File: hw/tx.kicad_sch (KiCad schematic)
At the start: 60 parts, among them Q301 MMBF170, Q302 MMBF170, Q303 MMBF170, Q304 MMBF170, Q305 MMBF170, Q306 MMBF170, Q307 MMBF170, Q308 MMBF170, Q309 MMBF170, Q310 MMBF170, Q311 MMBF170, Q312 MMBF170, T301 BN-43-202_DualPri_CTSec, U301 ICE40UP5K-SG48ITR, U302 CD74ACT541SM96, Y301 40MHz

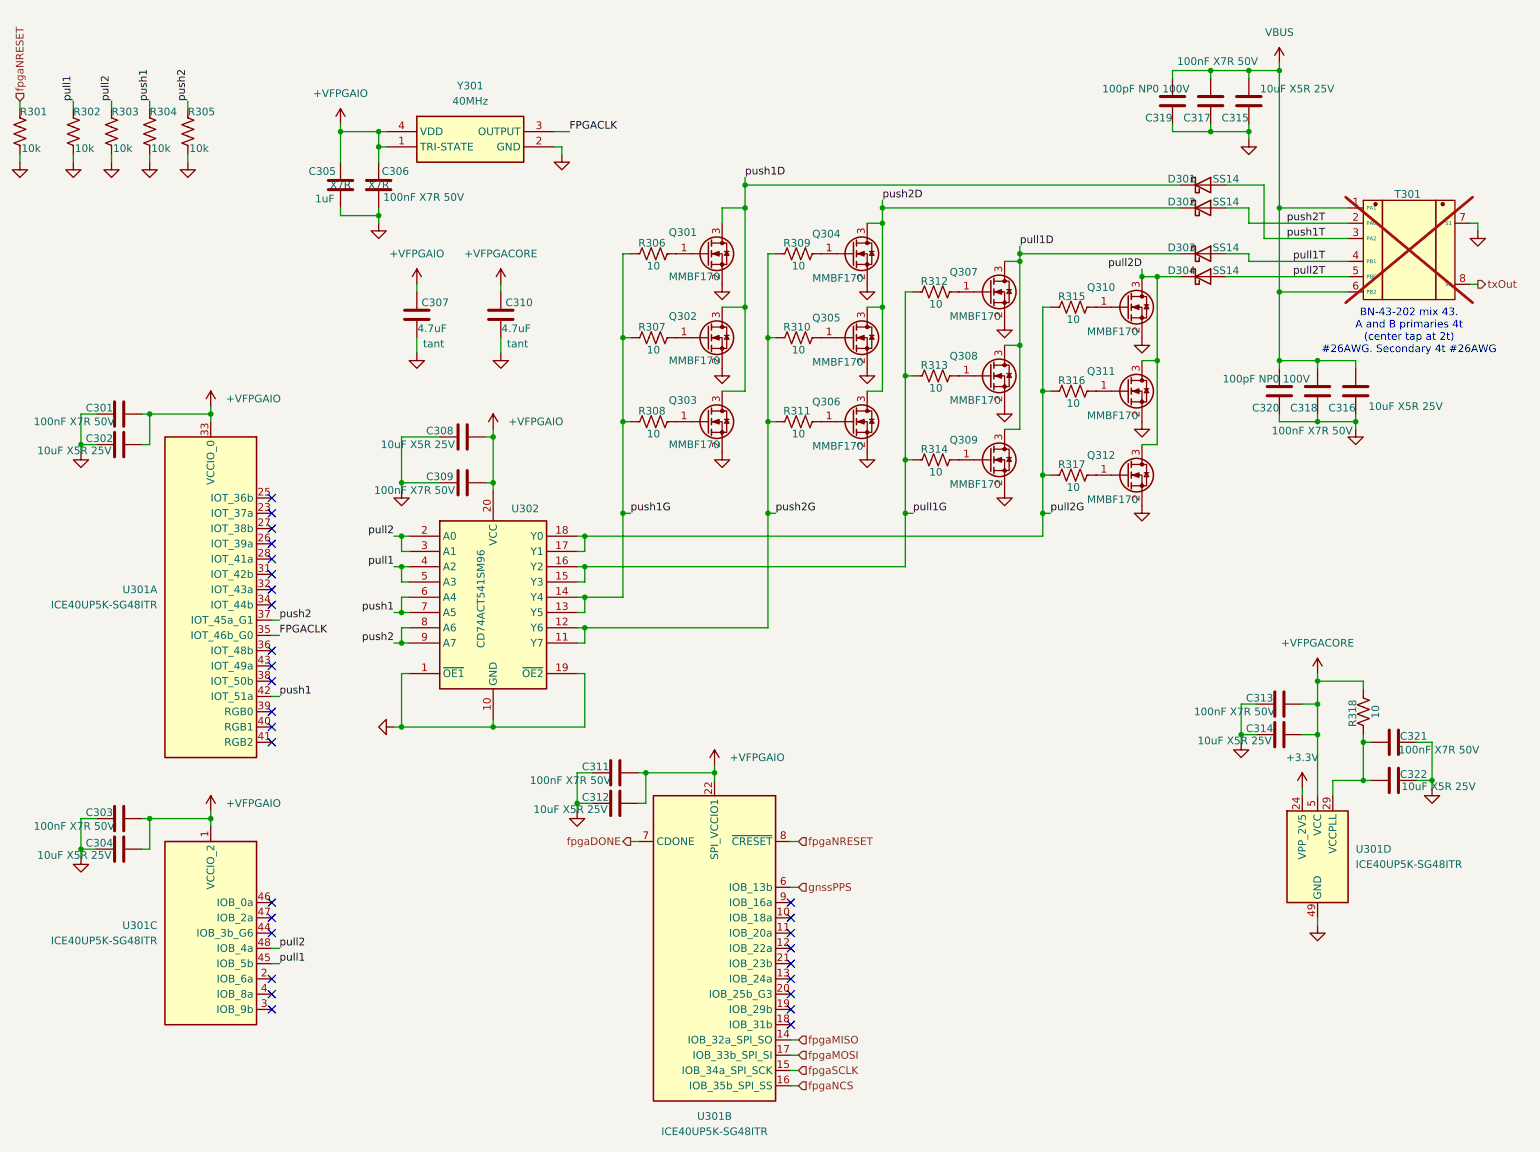
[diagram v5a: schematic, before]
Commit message: Still working on FPGA config loading. Problem is now CMOS lockup caused by FPGACORE vs FPGAIO rails. I moved FPGAIO enable to IO42 on ESP32 and pgFPGACORE to IO41.
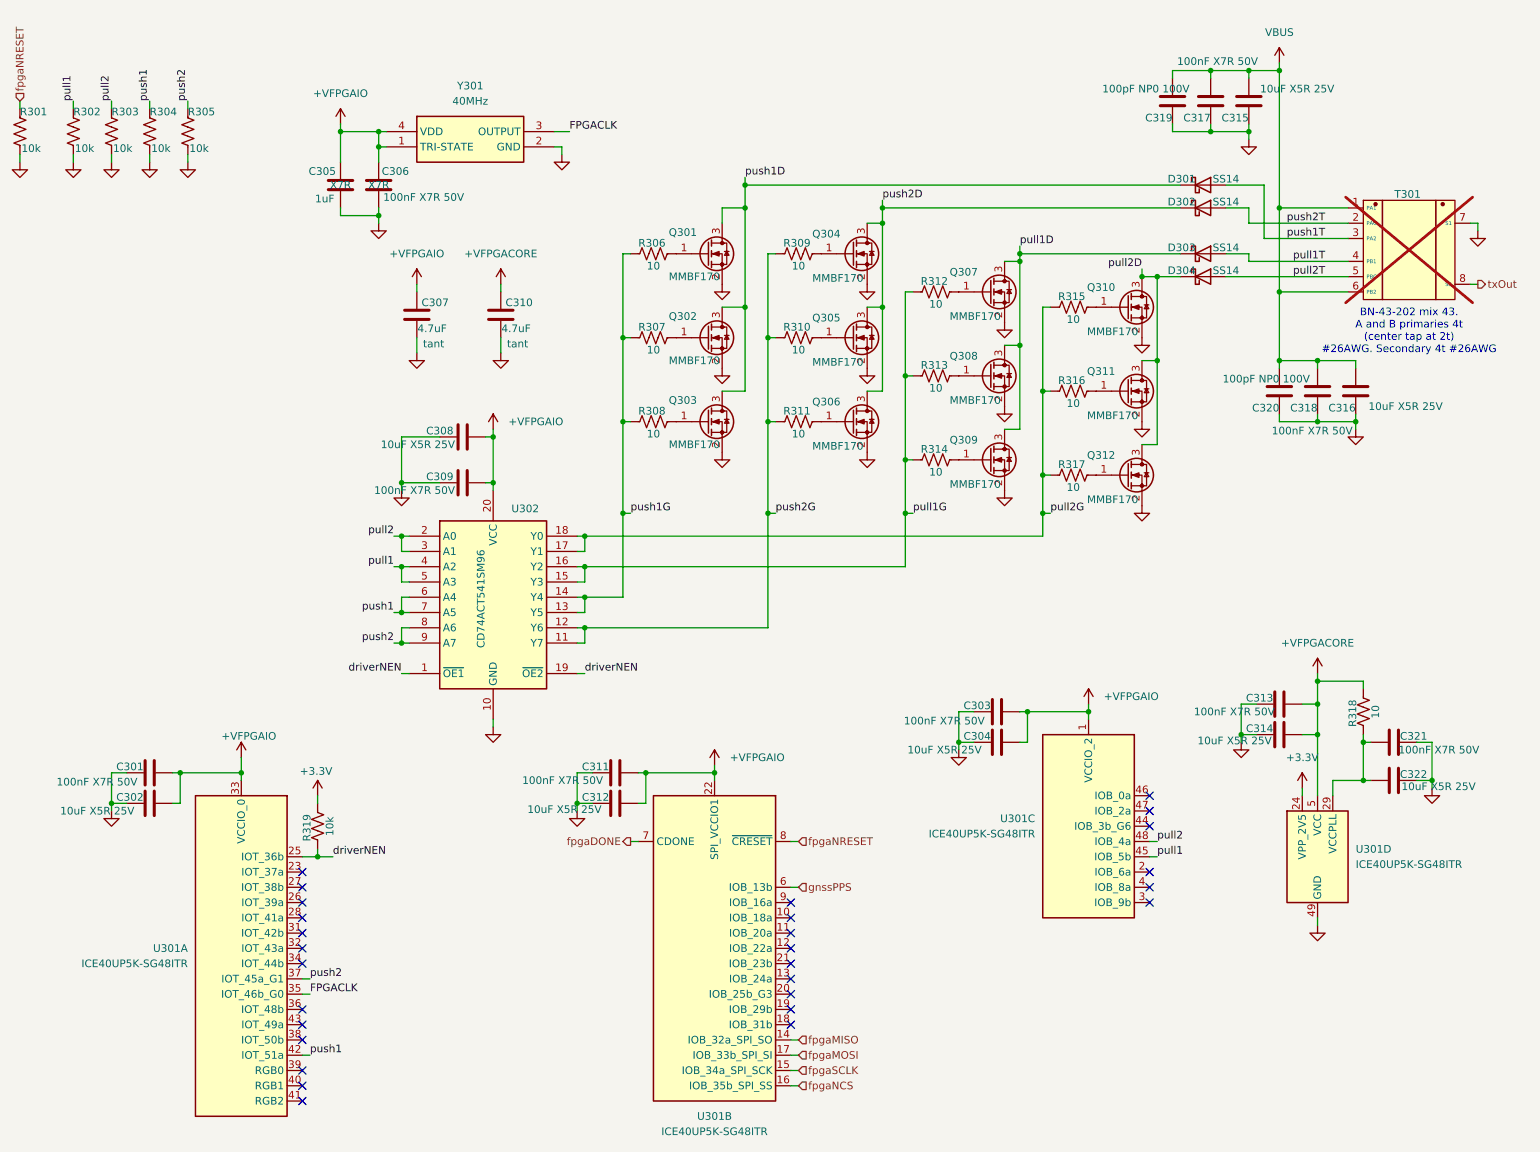
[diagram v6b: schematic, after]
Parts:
- added R319: 10k, Resistor_SMD:R_0402_1005Metric, symbol Device:R_US
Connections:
- net +3.3V: now also R319.2
- net GND: no longer U302.1 (~{OE1}), U302.19 (~{OE2})
- net driverNEN: now reaches U301.25 (IOT_36b)
- net driverNEN: now also U302.1 (~{OE1}), U302.19 (~{OE2}), R319.1
- no-connect marks 29 -> 28
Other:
- moved on the sheet: C301, C302, C303, C304, U301A, U301C
